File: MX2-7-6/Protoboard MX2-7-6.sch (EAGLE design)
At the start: 294 parts

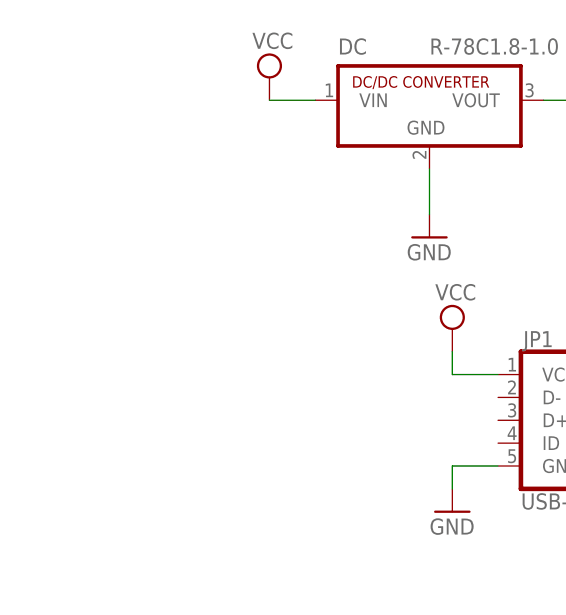
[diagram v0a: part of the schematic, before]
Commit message: Update Gerb files
Created Gerber files for MX 2-7-6 without ESP
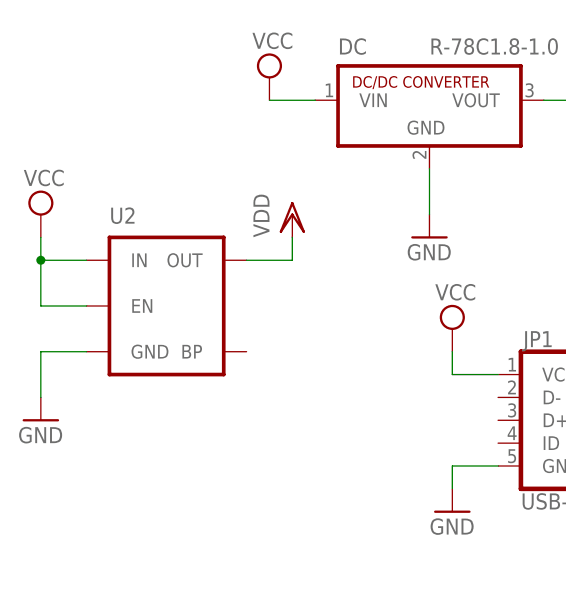
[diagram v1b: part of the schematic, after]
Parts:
- added U2: (no value), SparkFun-PowerIC:MIC52053.3V
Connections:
- net GND: now also U2.GND
- net VCC: now also U2.EN, U2.IN
- net VDD: now also U2.OUT
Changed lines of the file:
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@@
 <?xml version="1.0" encoding="utf-8"?>
 <!DOCTYPE eagle SYSTEM "eagle.dtd">
-<eagle version="7.6.0">
+<eagle version="7.7.0">
 <drawing>
 <settings>
@@
 <part name="SUPPLY1" library="supply2" deviceset="VCC" device=""/>
 <part name="GND3" library="supply1" deviceset="GND" device=""/>
+<part name="SUPPLY2" library="supply2" deviceset="VCC" device=""/>
+<part name="GND5" library="supply1" deviceset="GND" device=""/>
+<part name="VDD4" library="supply1" deviceset="VDD" device=""/>
+<part name="U2" library="SparkFun-PowerIC" deviceset="MIC5205" device="3.3V"/>
 </parts>
 <sheets>
@@
 <instance part="SUPPLY1" gate="G$1" x="-25.4" y="38.1"/>
 <instance part="GND3" gate="1" x="-25.4" y="17.78"/>
+<instance part="SUPPLY2" gate="G$1" x="-71.12" y="50.8"/>
+<instance part="GND5" gate="1" x="-71.12" y="27.94"/>
+<instance part="VDD4" gate="G$1" x="-43.18" y="50.8"/>
+<instance part="U2" gate="G$1" x="-55.88" y="40.64"/>
 </instances>
 <busses>
@@
 <wire x1="-25.4" y1="22.86" x2="-25.4" y2="20.32" width="0.1524" layer="91"/>
 </segment>
+<segment>
+<pinref part="GND5" gate="1" pin="GND"/>
+<wire x1="-71.12" y1="30.48" x2="-71.12" y2="35.56" width="0.1524" layer="91"/>
+<pinref part="U2" gate="G$1" pin="GND"/>
+<wire x1="-71.12" y1="35.56" x2="-66.04" y2="35.56" width="0.1524" layer="91"/>
+</segment>
 </net>
 <net name="VCC" class="0">
@@
 <wire x1="-20.32" y1="33.02" x2="-25.4" y2="33.02" width="0.1524" layer="91"/>
 <wire x1="-25.4" y1="33.02" x2="-25.4" y2="35.56" width="0.1524" layer="91"/>
+</segment>
+<segment>
+<pinref part="U2" gate="G$1" pin="EN"/>
+<pinref part="SUPPLY2" gate="G$1" pin="VCC"/>
+<wire x1="-66.04" y1="40.64" x2="-71.12" y2="40.64" width="0.1524" layer="91"/>
+<wire x1="-71.12" y1="40.64" x2="-71.12" y2="45.72" width="0.1524" layer="91"/>
+<pinref part="U2" gate="G$1" pin="IN"/>
+<wire x1="-71.12" y1="45.72" x2="-71.12" y2="48.26" width="0.1524" layer="91"/>
+<wire x1="-66.04" y1="45.72" x2="-71.12" y2="45.72" width="0.1524" layer="91"/>
+<junction x="-71.12" y="45.72"/>
 </segment>
 </net>
@@
 <wire x1="17.78" y1="55.88" x2="17.78" y2="43.18" width="0.1524" layer="91"/>
 </segment>
-</net>
+<segment>
+<pinref part="U2" gate="G$1" pin="OUT"/>
+<pinref part="VDD4" gate="G$1" pin="VDD"/>
+<wire x1="-48.26" y1="45.72" x2="-43.18" y2="45.72" width="0.1524" layer="91"/>
+<wire x1="-43.18" y1="45.72" x2="-43.18" y2="48.26" width="0.1524" layer="91"/>
+</segment>
+</net>

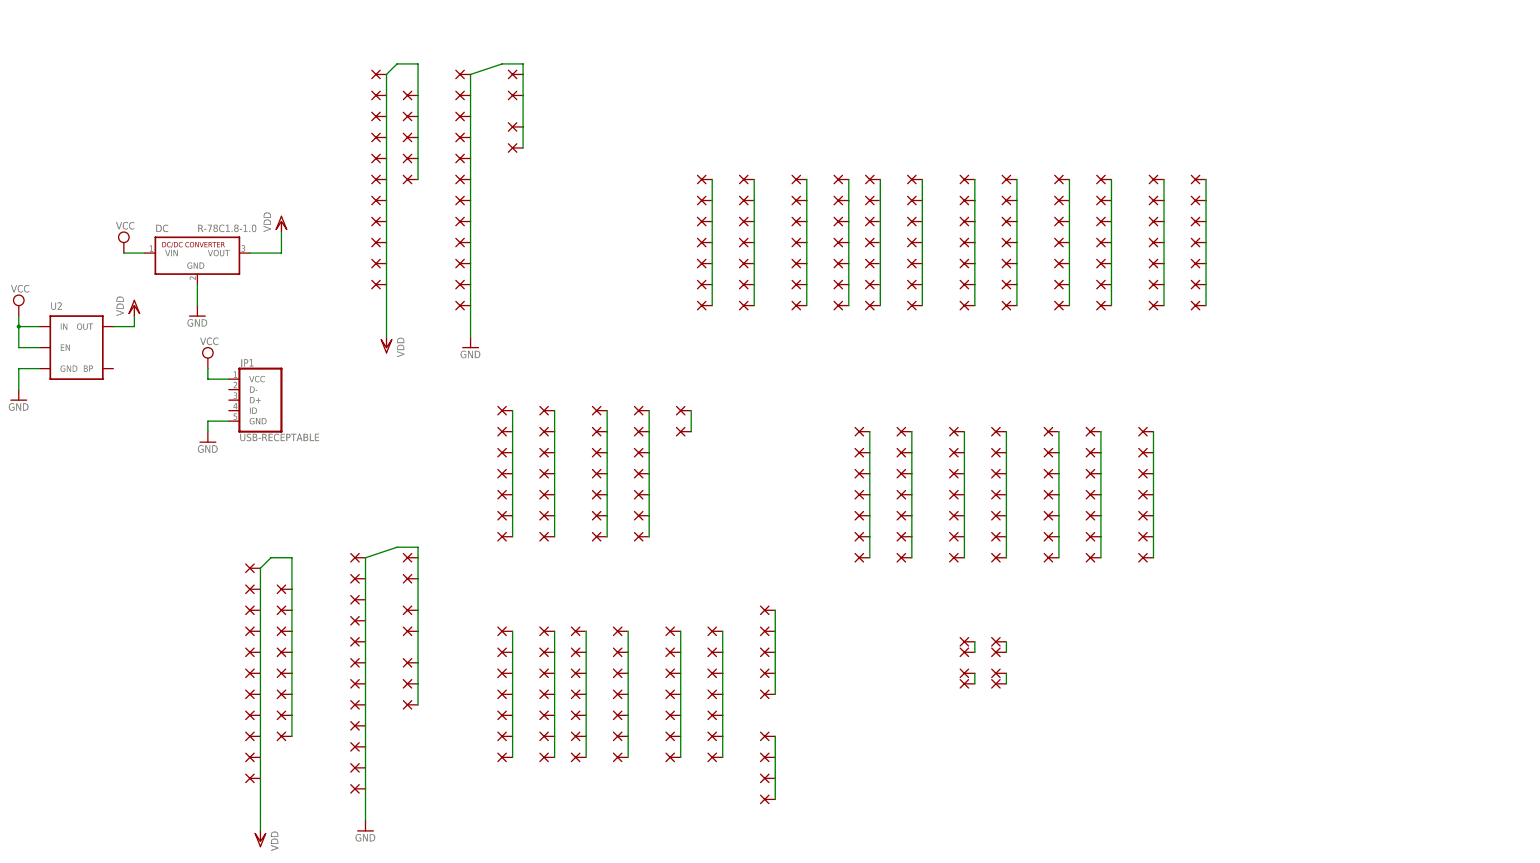
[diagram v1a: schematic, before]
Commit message: Update to rev2
Updated to Pin headers instead of single wire pads
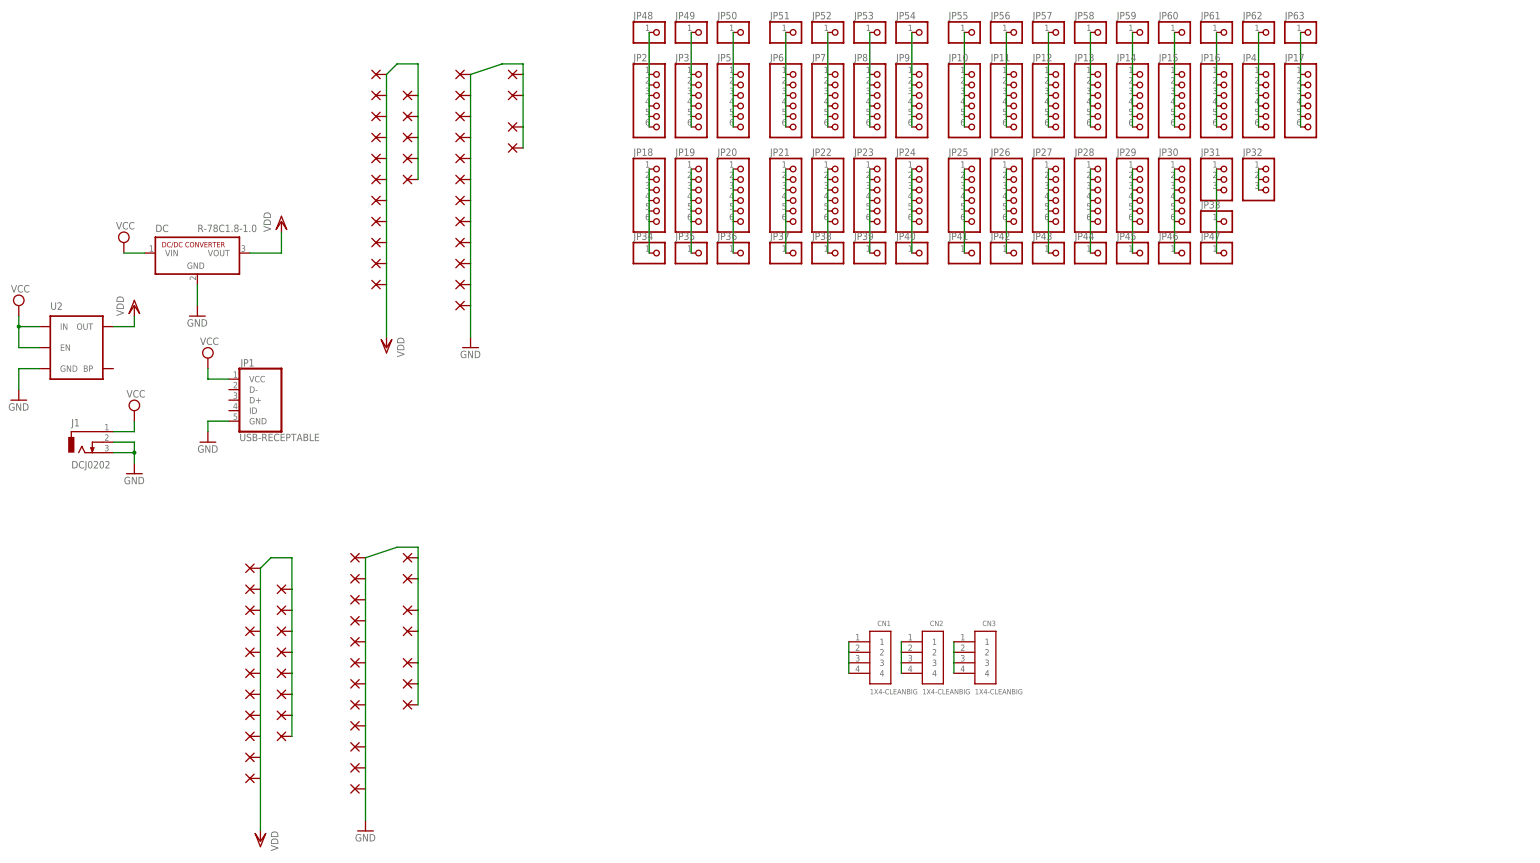
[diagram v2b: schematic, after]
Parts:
- removed PAD1, PAD100, PAD101, PAD102, PAD103, PAD106, PAD107, PAD108, PAD109, PAD110, PAD111, PAD112, PAD115, PAD116, PAD117, PAD118, PAD119, PAD120, PAD121, PAD124, PAD125, PAD126, PAD127, PAD128, PAD129, PAD130, PAD133, PAD134, PAD135, PAD136, PAD137, PAD138, PAD139, PAD142, PAD143, PAD144, PAD145, PAD146, PAD147, PAD148, PAD151, PAD152, PAD153, PAD154, PAD155, PAD156, PAD157, PAD160, PAD161, PAD162, PAD163, PAD164, PAD165, PAD166, PAD169, PAD170, PAD171, PAD172, PAD173, PAD174, PAD175, PAD178, PAD179, PAD180, PAD181, PAD182, PAD183, PAD184, PAD187, PAD188, PAD189, PAD190, PAD191, PAD192, PAD193, PAD196, PAD197, PAD198, PAD199, PAD2, PAD200, PAD201, PAD202, PAD205, PAD206, PAD207, PAD208, PAD209, PAD210, PAD211, PAD214, PAD215, PAD216, PAD217, PAD218, PAD219, PAD220, PAD260, PAD261, PAD262, PAD263, PAD264, PAD265, PAD266, PAD269, PAD270, PAD271, PAD272, PAD273, PAD274, PAD275, PAD278, PAD279, PAD280, PAD281, PAD282, PAD283, PAD284, PAD287, PAD288, PAD289, PAD290, PAD291, PAD292, PAD293, PAD296, PAD297, PAD298, PAD299, PAD300, PAD301, PAD302, PAD305, PAD306, PAD307, PAD308, PAD309, PAD310, PAD311, PAD314, PAD315, PAD316, PAD317, PAD318, PAD319, PAD320, PAD332, PAD333, PAD334, PAD335, PAD336, PAD337, PAD338, PAD341, PAD342, PAD343, PAD344, PAD345, PAD346, PAD347, PAD350, PAD351, PAD352, PAD353, PAD354, PAD355, PAD356, PAD359, PAD360, PAD361, PAD362, PAD363, PAD364, PAD365, PAD368, PAD369, PAD370, PAD371, PAD372, PAD373, PAD374, PAD377, PAD378, PAD379, PAD380, PAD381, PAD382, PAD383, PAD385, PAD386, PAD387, PAD388, PAD389, PAD391, PAD392, PAD393, PAD394, PAD79, PAD80, PAD81, PAD82, PAD83, PAD84, PAD85, PAD88, PAD89, PAD90, PAD91, PAD92, PAD93, PAD94, PAD97, PAD98, PAD99: (no value), wirepad:1,6/0,8
- removed PAD34, PAD35, PAD39, PAD40, PAD42, PAD43, PAD45, PAD46: (no value), wirepad:3,17/1,3
- added CN1, CN2, CN3: 1X4-CLEANBIG, adafruit:1X4-CLEANBIG
- added J1: DCJ0202, con-jack:DCJ0202
- added JP10, JP11, JP12, JP13, JP14, JP15, JP16, JP17, JP18, JP19, JP2, JP20, JP21, JP22, JP23, JP24, JP25, JP26, JP27, JP28, JP29, JP3, JP30, JP4, JP5, JP6, JP7, JP8, JP9: (no value), adafruit:PINHD-1X6CB
- added JP31, JP32: (no value), adafruit:PINHD-1X3CB
- added JP33, JP34, JP35, JP36, JP37, JP38, JP39, JP40, JP41, JP42, JP43, JP44, JP45, JP46, JP47, JP48, JP49, JP50, JP51, JP52, JP53, JP54, JP55, JP56, JP57, JP58, JP59, JP60, JP61, JP62, JP63: (no value), adafruit:PINHD-1X1CB
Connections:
- removed net N$40: PAD377.P, PAD378.P, PAD379.P, PAD380.P, PAD381.P, PAD382.P, PAD383.P
- removed net N$41: PAD385.P, PAD386.P, PAD387.P, PAD388.P, PAD389.P
- net GND: now also J1.2, J1.3
- net N$1: now also JP2.1, JP2.2, JP2.3, JP2.4, JP2.5, JP2.6, JP48.1; no longer PAD391.P, PAD392.P, PAD393.P, PAD394.P
- net N$10: now also JP54.1, JP9.1, JP9.2, JP9.3, JP9.4, JP9.5, JP9.6; no longer PAD106.P, PAD107.P, PAD108.P, PAD109.P, PAD110.P, PAD111.P, PAD112.P
- net N$11: now also JP10.1, JP10.2, JP10.3, JP10.4, JP10.5, JP10.6, JP55.1; no longer PAD115.P, PAD116.P, PAD117.P, PAD118.P, PAD119.P, PAD120.P, PAD121.P
- net N$12: now also JP11.1, JP11.2, JP11.3, JP11.4, JP11.5, JP11.6, JP56.1; no longer PAD124.P, PAD125.P, PAD126.P, PAD127.P, PAD128.P, PAD129.P, PAD130.P
- net N$13: now also JP12.1, JP12.2, JP12.3, JP12.4, JP12.5, JP12.6, JP57.1; no longer PAD133.P, PAD134.P, PAD135.P, PAD136.P, PAD137.P, PAD138.P, PAD139.P
- net N$14: now also JP13.1, JP13.2, JP13.3, JP13.4, JP13.5, JP13.6, JP58.1; no longer PAD142.P, PAD143.P, PAD144.P, PAD145.P, PAD146.P, PAD147.P, PAD148.P
- net N$15: now also JP14.1, JP14.2, JP14.3, JP14.4, JP14.5, JP14.6, JP59.1; no longer PAD151.P, PAD152.P, PAD153.P, PAD154.P, PAD155.P, PAD156.P, PAD157.P
- net N$16: now also JP15.1, JP15.2, JP15.3, JP15.4, JP15.5, JP15.6, JP60.1; no longer PAD160.P, PAD161.P, PAD162.P, PAD163.P, PAD164.P, PAD165.P, PAD166.P
- net N$17: now also JP16.1, JP16.2, JP16.3, JP16.4, JP16.5, JP16.6, JP61.1; no longer PAD169.P, PAD170.P, PAD171.P, PAD172.P, PAD173.P, PAD174.P, PAD175.P
- net N$18: now also JP4.1, JP4.2, JP4.3, JP4.4, JP4.5, JP4.6, JP62.1; no longer PAD178.P, PAD179.P, PAD180.P, PAD181.P, PAD182.P, PAD183.P, PAD184.P
- net N$19: now also JP17.1, JP17.2, JP17.3, JP17.4, JP17.5, JP17.6, JP63.1; no longer PAD187.P, PAD188.P, PAD189.P, PAD190.P, PAD191.P, PAD192.P, PAD193.P
- net N$2: now also CN1.1, CN1.2, CN1.3, CN1.4; no longer PAD34.P, PAD35.P
- net N$20: now also JP18.1, JP18.2, JP18.3, JP18.4, JP18.5, JP18.6, JP34.1; no longer PAD196.P, PAD197.P, PAD198.P, PAD199.P, PAD200.P, PAD201.P, PAD202.P
- net N$21: now also JP19.1, JP19.2, JP19.3, JP19.4, JP19.5, JP19.6, JP35.1; no longer PAD205.P, PAD206.P, PAD207.P, PAD208.P, PAD209.P, PAD210.P, PAD211.P
- net N$22: now also JP20.1, JP20.2, JP20.3, JP20.4, JP20.5, JP20.6, JP36.1; no longer PAD214.P, PAD215.P, PAD216.P, PAD217.P, PAD218.P, PAD219.P, PAD220.P
- net N$27: now also JP21.1, JP21.2, JP21.3, JP21.4, JP21.5, JP21.6, JP37.1; no longer PAD260.P, PAD261.P, PAD262.P, PAD263.P, PAD264.P, PAD265.P, PAD266.P
- net N$28: now also JP22.1, JP22.2, JP22.3, JP22.4, JP22.5, JP22.6, JP38.1; no longer PAD269.P, PAD270.P, PAD271.P, PAD272.P, PAD273.P, PAD274.P, PAD275.P
- net N$29: now also JP23.1, JP23.2, JP23.3, JP23.4, JP23.5, JP23.6, JP39.1; no longer PAD278.P, PAD279.P, PAD280.P, PAD281.P, PAD282.P, PAD283.P, PAD284.P
- net N$3: now also CN2.1, CN2.2, CN2.3, CN2.4; no longer PAD1.P, PAD2.P
- net N$30: now also JP24.1, JP24.2, JP24.3, JP24.4, JP24.5, JP24.6, JP40.1; no longer PAD287.P, PAD288.P, PAD289.P, PAD290.P, PAD291.P, PAD292.P, PAD293.P
- net N$31: now also JP25.1, JP25.2, JP25.3, JP25.4, JP25.5, JP25.6, JP41.1; no longer PAD296.P, PAD297.P, PAD298.P, PAD299.P, PAD300.P, PAD301.P, PAD302.P
- net N$32: now also JP26.1, JP26.2, JP26.3, JP26.4, JP26.5, JP26.6, JP42.1; no longer PAD305.P, PAD306.P, PAD307.P, PAD308.P, PAD309.P, PAD310.P, PAD311.P
- net N$33: now also JP27.1, JP27.2, JP27.3, JP27.4, JP27.5, JP27.6, JP43.1; no longer PAD314.P, PAD315.P, PAD316.P, PAD317.P, PAD318.P, PAD319.P, PAD320.P
- net N$35: now also JP28.1, JP28.2, JP28.3, JP28.4, JP28.5, JP28.6, JP44.1; no longer PAD332.P, PAD333.P, PAD334.P, PAD335.P, PAD336.P, PAD337.P, PAD338.P
- net N$36: now also JP29.1, JP29.2, JP29.3, JP29.4, JP29.5, JP29.6, JP45.1; no longer PAD341.P, PAD342.P, PAD343.P, PAD344.P, PAD345.P, PAD346.P, PAD347.P
- net N$37: now also JP30.1, JP30.2, JP30.3, JP30.4, JP30.5, JP30.6, JP46.1; no longer PAD350.P, PAD351.P, PAD352.P, PAD353.P, PAD354.P, PAD355.P, PAD356.P
- net N$38: now also JP31.1, JP31.2, JP31.3, JP33.1, JP47.1; no longer PAD359.P, PAD360.P, PAD361.P, PAD362.P, PAD363.P, PAD364.P, PAD365.P
- net N$39: now also JP32.1, JP32.2, JP32.3; no longer PAD368.P, PAD369.P, PAD370.P, PAD371.P, PAD372.P, PAD373.P, PAD374.P
- net N$4: now also CN3.1, CN3.2, CN3.3, CN3.4; no longer PAD39.P, PAD40.P
- net N$5: now also JP3.1, JP3.2, JP3.3, JP3.4, JP3.5, JP3.6, JP49.1; no longer PAD42.P, PAD43.P
- net N$6: now also JP5.1, JP5.2, JP5.3, JP5.4, JP5.5, JP5.6, JP50.1; no longer PAD45.P, PAD46.P
- net N$7: now also JP51.1, JP6.1, JP6.2, JP6.3, JP6.4, JP6.5, JP6.6; no longer PAD79.P, PAD80.P, PAD81.P, PAD82.P, PAD83.P, PAD84.P, PAD85.P
- net N$8: now also JP52.1, JP7.1, JP7.2, JP7.3, JP7.4, JP7.5, JP7.6; no longer PAD88.P, PAD89.P, PAD90.P, PAD91.P, PAD92.P, PAD93.P, PAD94.P
- net N$9: now also JP53.1, JP8.1, JP8.2, JP8.3, JP8.4, JP8.5, JP8.6; no longer PAD100.P, PAD101.P, PAD102.P, PAD103.P, PAD97.P, PAD98.P, PAD99.P
- net VCC: now also J1.1

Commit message: Change usb connector
Change to correct usb connecter and moved esp8266 bit more onto the
board.
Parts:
- removed JP1: USB-RECEPTABLE, daspilker:USB-RECEPTABLE
- added X1: (no value), microbuilder:USBMICRO_20329
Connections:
- net GND: now also X1.GND; no longer JP1.GND
- net VCC: now also X1.VBUS; no longer JP1.VCC
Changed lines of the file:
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@@
 <part name="PAD38" library="wirepad" deviceset="1,6/0,8" device=""/>
 <part name="GND1" library="supply1" deviceset="GND" device=""/>
-<part name="JP1" library="daspilker" deviceset="USB-RECEPTABLE" device=""/>
-<part name="SUPPLY1" library="supply2" deviceset="VCC" device=""/>
-<part name="GND3" library="supply1" deviceset="GND" device=""/>
 <part name="SUPPLY2" library="supply2" deviceset="VCC" device=""/>
 <part name="GND5" library="supply1" deviceset="GND" device=""/>
@@
 <part name="JP62" library="adafruit" deviceset="PINHD-1X1" device="CB"/>
 <part name="JP63" library="adafruit" deviceset="PINHD-1X1" device="CB"/>
+<part name="X1" library="microbuilder" deviceset="USB" device="MICRO_20329"/>
+<part name="SUPPLY5" library="supply2" deviceset="VCC" device=""/>
+<part name="GND7" library="supply1" deviceset="GND" device=""/>
 </parts>
 <sheets>
@@
 </instance>
 <instance part="GND1" gate="1" x="38.1" y="40.64"/>
-<instance part="JP1" gate="G$1" x="-12.7" y="27.94"/>
-<instance part="SUPPLY1" gate="G$1" x="-25.4" y="38.1"/>
-<instance part="GND3" gate="1" x="-25.4" y="17.78"/>
 <instance part="SUPPLY2" gate="G$1" x="-71.12" y="50.8"/>
 <instance part="GND5" gate="1" x="-71.12" y="27.94"/>
@@
 <instance part="JP62" gate="G$1" x="231.14" y="116.84"/>
 <instance part="JP63" gate="G$1" x="241.3" y="116.84"/>
+<instance part="X1" gate="G$1" x="-53.34" y="-12.7"/>
+<instance part="SUPPLY5" gate="G$1" x="-40.64" y="-2.54"/>
+<instance part="GND7" gate="1" x="-40.64" y="-22.86"/>
 </instances>
 <busses>
@@
 </segment>
 <segment>
-<pinref part="JP1" gate="G$1" pin="GND"/>
-<pinref part="GND3" gate="1" pin="GND"/>
-<wire x1="-20.32" y1="22.86" x2="-25.4" y2="22.86" width="0.1524" layer="91"/>
-<wire x1="-25.4" y1="22.86" x2="-25.4" y2="20.32" width="0.1524" layer="91"/>
-</segment>
-<segment>
 <pinref part="GND5" gate="1" pin="GND"/>
 <wire x1="-71.12" y1="30.48" x2="-71.12" y2="35.56" width="0.1524" layer="91"/>
@@
 <junction x="-43.18" y="15.24"/>
 </segment>
+<segment>
+<pinref part="X1" gate="G$1" pin="GND"/>
+<pinref part="GND7" gate="1" pin="GND"/>
+<wire x1="-43.18" y1="-17.78" x2="-40.64" y2="-17.78" width="0.1524" layer="91"/>
+<wire x1="-40.64" y1="-17.78" x2="-40.64" y2="-20.32" width="0.1524" layer="91"/>
+</segment>
 </net>
 <net name="VCC" class="0">
@@
 <pinref part="DC" gate="G$1" pin="VIN"/>
 <wire x1="-45.72" y1="63.5" x2="-40.64" y2="63.5" width="0.1524" layer="91"/>
-</segment>
-<segment>
-<pinref part="JP1" gate="G$1" pin="VCC"/>
-<pinref part="SUPPLY1" gate="G$1" pin="VCC"/>
-<wire x1="-20.32" y1="33.02" x2="-25.4" y2="33.02" width="0.1524" layer="91"/>
-<wire x1="-25.4" y1="33.02" x2="-25.4" y2="35.56" width="0.1524" layer="91"/>
 </segment>
 <segment>
@@
 <wire x1="-43.18" y1="20.32" x2="-43.18" y2="22.86" width="0.1524" layer="91"/>
 </segment>
+<segment>
+<pinref part="X1" gate="G$1" pin="VBUS"/>
+<pinref part="SUPPLY5" gate="G$1" pin="VCC"/>
+<wire x1="-43.18" y1="-7.62" x2="-40.64" y2="-7.62" width="0.1524" layer="91"/>
+<wire x1="-40.64" y1="-7.62" x2="-40.64" y2="-5.08" width="0.1524" layer="91"/>
+</segment>
 </net>
